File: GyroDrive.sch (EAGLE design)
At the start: 32 parts, among them Q1 TF412ST5G, Q2 TF412ST5G, Q3 TF412ST5G, Q4 TF412ST5G, Q5 TF412ST5G, Q6 TF412ST5G

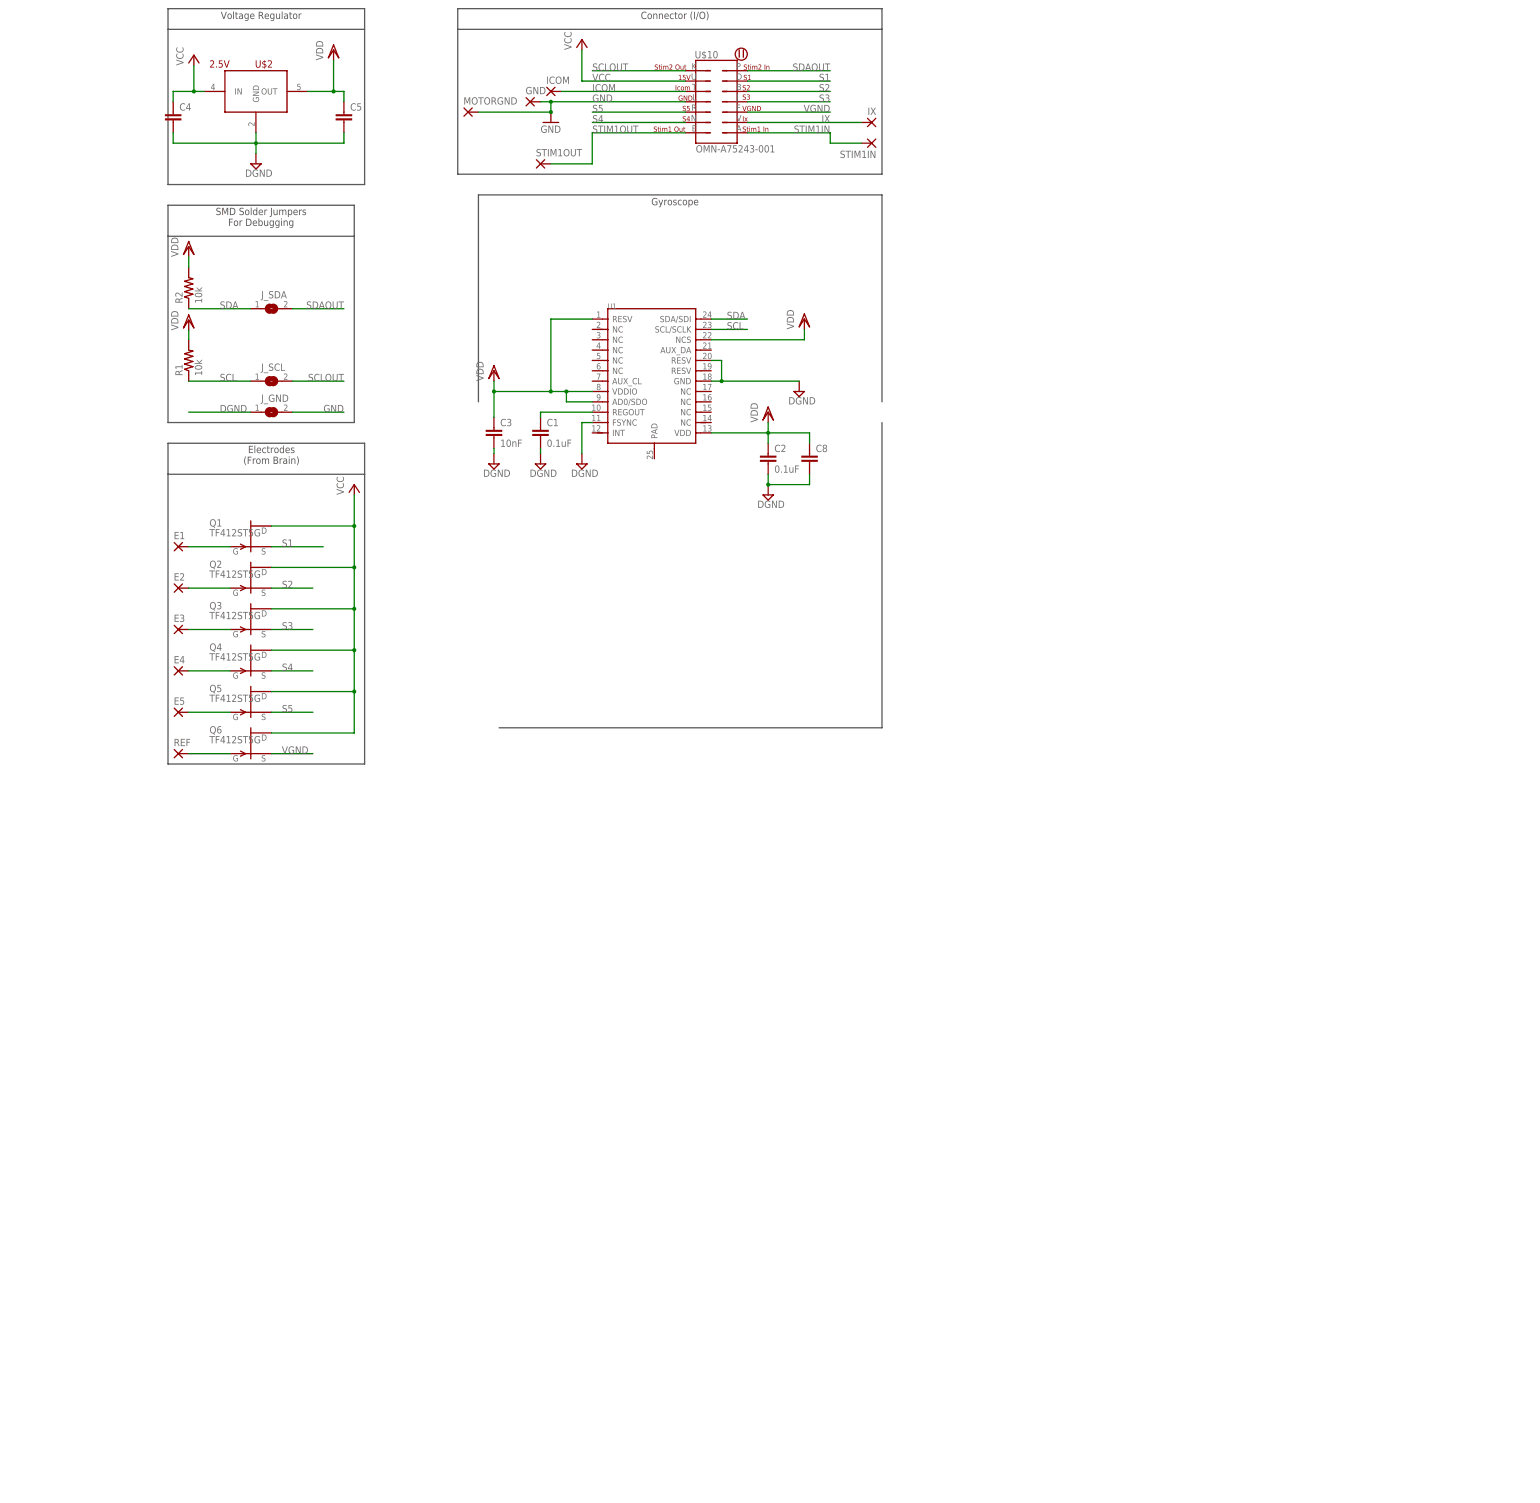
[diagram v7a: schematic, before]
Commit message: Added instrumentation amplifiers for neural signals
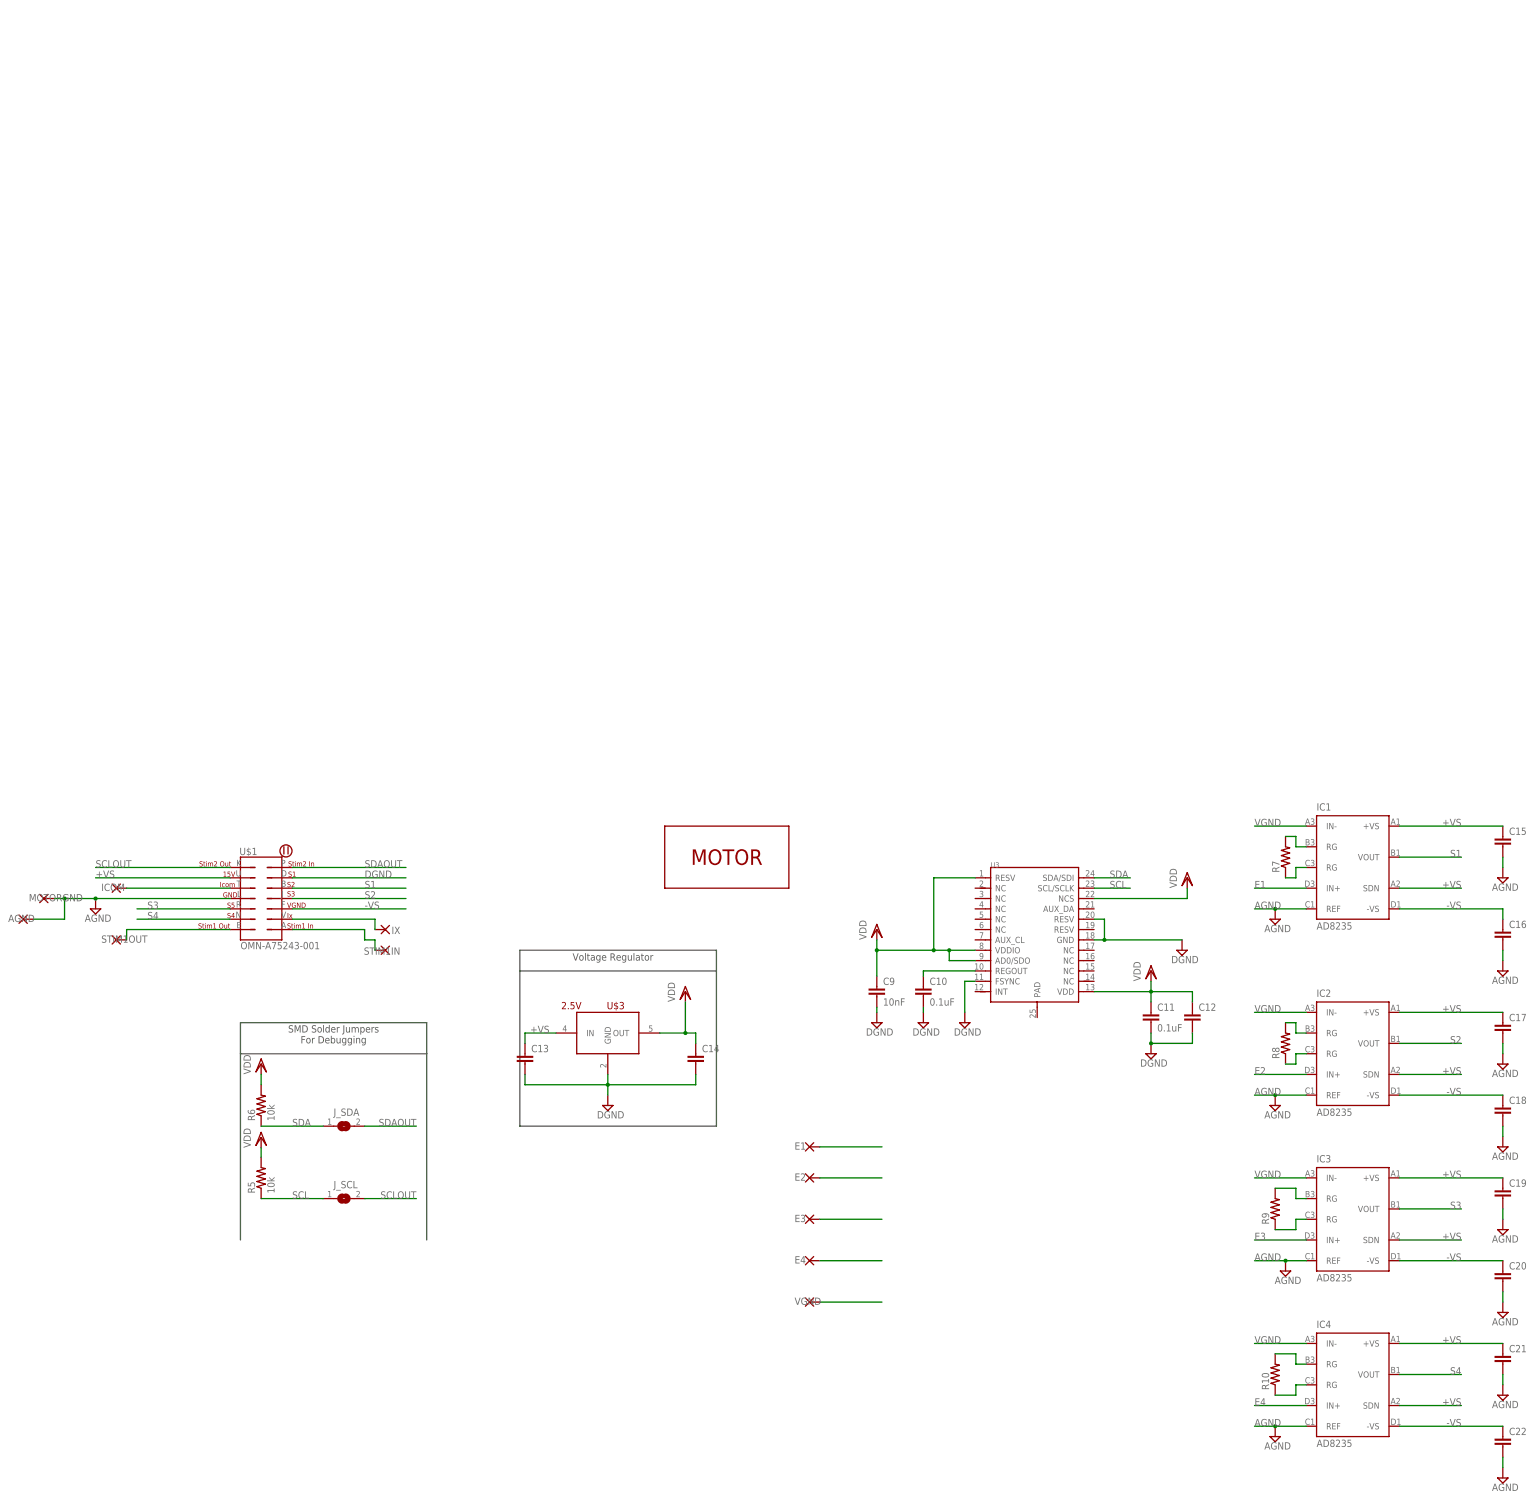
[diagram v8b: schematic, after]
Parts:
- removed C1, C2: 0.1uF, resistor:C-EUC0402
- removed C3: 10nF, resistor:C-EUC0402
- removed C4, C5: (no value), resistor:C-EUC0402
- removed C8: (no value), resistor:C-EUC0603
- removed E5, GND, REF: (no value), michael-stetner:THROUGH-HOLE-30MIL/15MIL
- removed J_GND: (no value), michael-stetner:SJ
- removed Q1, Q2, Q3, Q4, Q5, Q6: TF412ST5G, on-semiconductor-mes:TF412ST5G
- removed R1, R2: 10k, resistor:R-US_R0201
- removed U$10: OMN-A75243-001, GFL:OMN-A75243-001
- removed U1: (no value), Grove - IMU 10DOF v1.1:MPU-9250
- added AGND, VGND: (no value), michael-stetner:THROUGH-HOLE-30MIL/15MIL
- added C10, C11: 0.1uF, resistor:C-EUC0402
- added C12: (no value), resistor:C-EUC0603
- added C13, C14: (no value), resistor:C-EUC0402
- added C15, C16, C17, C18, C19, C20, C21, C22: (no value), resistor:C-EUC0201
- added C9: 10nF, resistor:C-EUC0402
- added IC1, IC2, IC3, IC4: AD8235, analog-devices:AD8235
- added R10, R7, R8, R9: (no value), resistor:R-US_R0201
- added R5, R6: 10k, resistor:R-US_R0201
- added U$1: OMN-A75243-001, GFL:OMN-A75243-001
- added U$3: 2.5V, michael-stetner:TPS715-FIXED
- added U3: (no value), Grove - IMU 10DOF v1.1:MPU-9250
- ICOM, IX, MOTORGND: device wirepad:1,6/0,8 -> michael-stetner:THROUGH-HOLE-30MIL/15MIL
- U$2: value 2.5V -> MICRODRIVE-MOTOR; device michael-stetner:TPS715-FIXED -> michael-stetner:MICRODRIVE-MOTOR
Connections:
- removed net GND: GND.P, J_GND.2, MOTORGND.P, U$10.L
- removed net ICOM: ICOM.P, U$10.T
- removed net IX: IX.P, U$10.V
- removed net N$10: E1.P, Q1.G
- removed net N$2: C1.1, U1.REGOUT
- removed net N$4: Q6.G, REF.P
- removed net N$5: E5.P, Q5.G
- removed net N$6: E4.P, Q4.G
- removed net N$8: E2.P, Q2.G
- removed net S5: Q5.S, U$10.R
- removed net STIM1IN: STIM1IN.P, U$10.A
- removed net STIM1OUT: STIM1OUT.P, U$10.E
- removed net VCC: C4.1, Q1.D, Q2.D, Q3.D, Q4.D, Q5.D, Q6.D, U$10.U, U$2.IN
- new net +VS: C13.1, C15.1, C17.1, C19.1, C21.1, IC1.+VS, IC1.SDN, IC2.+VS, IC2.SDN, IC3.+VS, IC3.SDN, IC4.+VS, IC4.SDN, U$1.U, U$3.IN
- new net -VS: C16.1, C18.1, C20.1, C22.1, IC1.-VS, IC2.-VS, IC3.-VS, IC4.-VS, U$1.F
- new net AGND: AGND.P, C15.2, C16.2, C17.2, C18.2, C19.2, C20.2, C21.2, C22.2, IC1.REF, IC2.REF, IC3.REF, IC4.REF, MOTORGND.P, U$1.L
- new net E1: E1.P, IC1.IN+
- new net E2: E2.P, IC2.IN+
- new net E3: E3.P, IC3.IN+
- new net E4: E4.P, IC4.IN+
- new net N$14: IX.P, U$1.V
- new net N$15: STIM1IN.P, U$1.A
- new net N$16: STIM1OUT.P, U$1.E
- new net N$17: ICOM.P, U$1.T
- new net N$18: IC1.RG@1, R7.1
- new net N$19: IC1.RG@2, R7.2
- new net N$20: IC2.RG@2, R8.2
- new net N$21: IC2.RG@1, R8.1
- new net N$22: IC3.RG@2, R9.2
- new net N$23: IC3.RG@1, R9.1
- new net N$24: IC4.RG@2, R10.2
- new net N$25: IC4.RG@1, R10.1
- net DGND: now also C10.2, C11.2, C12.2, C13.2, C14.2, C9.2, U$1.D, U$3.GND, U3.FSYNC, U3.GND, U3.RESV@2; no longer C1.2, C2.2, C3.2, C4.2, C5.2, C8.2, J_GND.1, U$2.GND, U1.FSYNC, U1.GND, U1.RESV@2
- net N$7: now also C10.1, U3.REGOUT; no longer E3.P, Q3.G
- net S1: now also IC1.VOUT, U$1.B; no longer Q1.S, U$10.D
- net S2: now also IC2.VOUT, U$1.J; no longer Q2.S, U$10.B
- net S3: now also IC3.VOUT, U$1.R; no longer Q3.S, U$10.J
- net S4: now also IC4.VOUT, U$1.N; no longer Q4.S, U$10.N
- net SCL: now also R5.1, U3.SCL/SCLK; no longer R1.1, U1.SCL/SCLK
- net SCLOUT: now also U$1.K; no longer U$10.K
- net SDA: now also R6.1, U3.SDA/SDI; no longer R2.1, U1.SDA/SDI
- net SDAOUT: now also U$1.P; no longer U$10.P
- net VDD: now also C11.1, C12.1, C14.1, C9.1, R5.2, R6.2, U$3.OUT, U3.AD0/SDO, U3.NCS, U3.RESV, U3.VDD, U3.VDDIO; no longer C2.1, C3.1, C5.1, C8.1, R1.2, R2.2, U$2.OUT, U1.AD0/SDO, U1.NCS, U1.RESV, U1.VDD, U1.VDDIO
- net VGND: now also IC1.IN-, IC2.IN-, IC3.IN-, IC4.IN-, VGND.P; no longer Q6.S, U$10.F
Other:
- note removed: "Connector (I/O)"
- note removed: "Electrodes (From Brain)"
- note removed: "Gyroscope"
- moved on the sheet: E1, E2, E3, E4, ICOM, IX, J_SCL, J_SDA, MOTORGND, STIM1IN, STIM1OUT
